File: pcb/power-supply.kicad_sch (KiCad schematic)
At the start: 10 parts, among them J1 Screw Connector, J2 Screw Connector, J3 Screw Connector, J4 Screw Connector, U9 NCP718BSNADJT1G

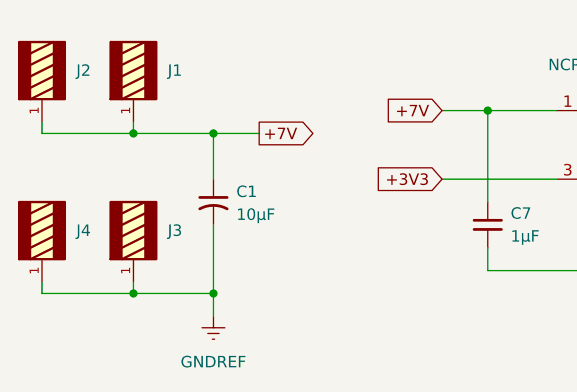
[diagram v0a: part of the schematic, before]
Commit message: Add header labels for UART and 3.3V
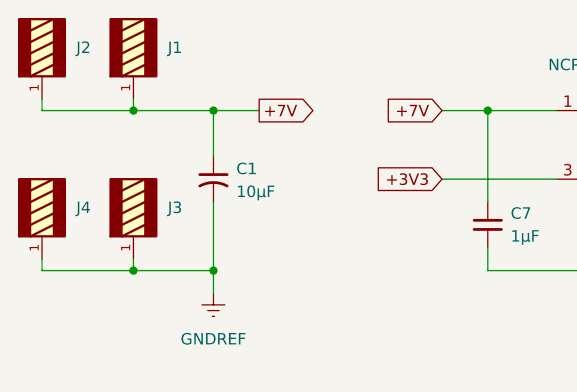
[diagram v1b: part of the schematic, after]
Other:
- company: (none) -> ECE 4710 - Vision Arm
- title: (none) -> 7V and 5V Power Supplies
- moved on the sheet: C1, J1, J2, J3, J4

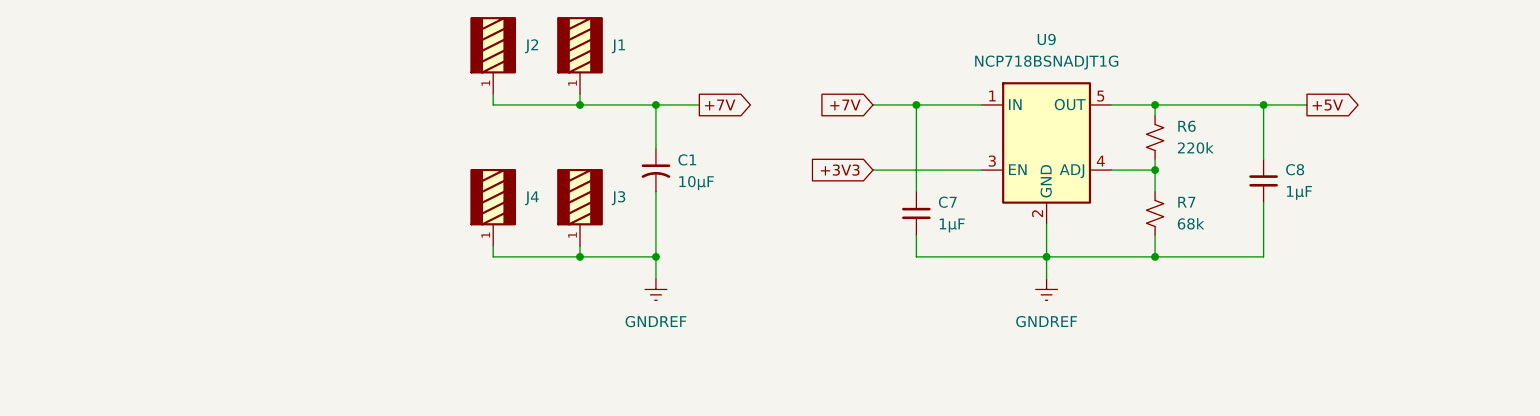
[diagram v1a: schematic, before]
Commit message: Add jumper to choose 3.3V or 7V for regulator enable
I'm not sure if using the 7V input voltage is alright, or if 7V is too
high. The datasheet for the LDO regulator `NCP718BSNADJT1G` doesn't seem
to make it clear, so the jumper lets us keep this same PCB design
without ordering a new board.
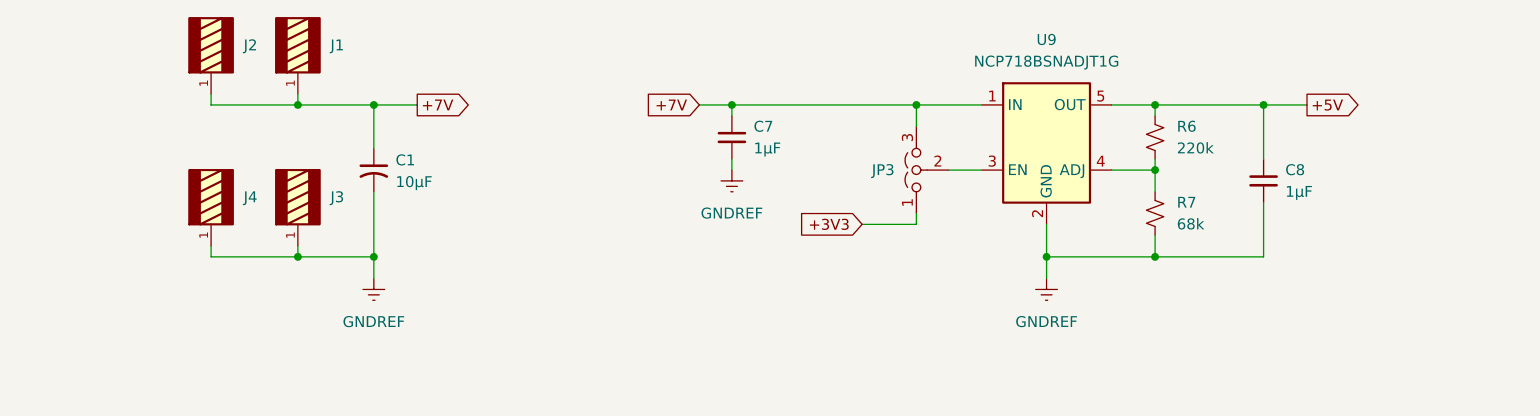
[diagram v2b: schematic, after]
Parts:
- added JP3: Jumper_3_Open, symbol Jumper:Jumper_3_Open
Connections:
- net +3V3: now also JP3.1 (A); no longer U9.3 (EN)
- net +7V: now also JP3.3 (B)
- new net: JP3.2 (C), U9.3 (EN)
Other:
- moved on the sheet: C1, J1, J2, J3, J4

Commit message: Change screw terminal to cheaper model
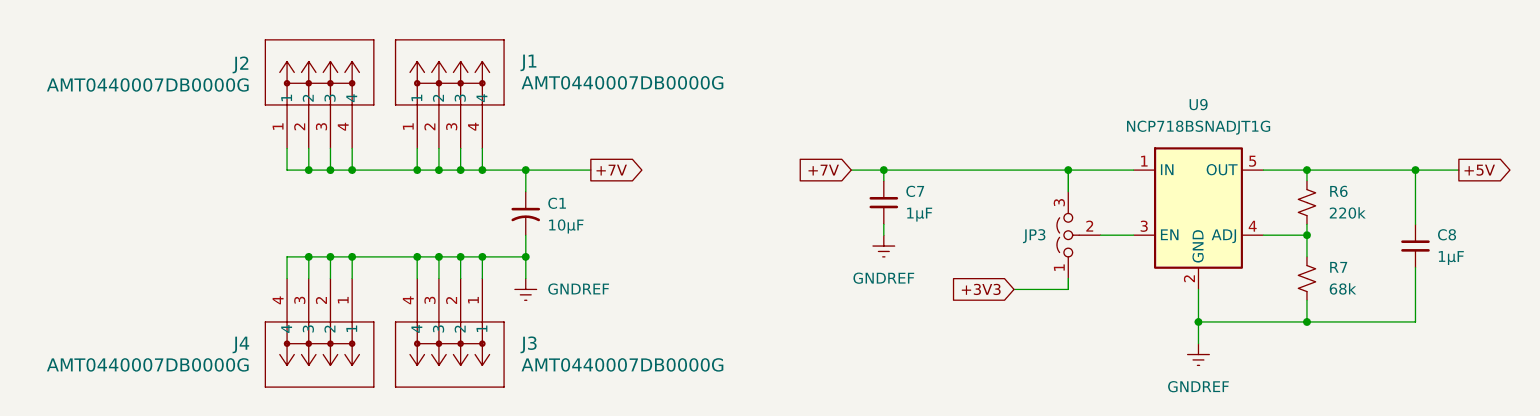
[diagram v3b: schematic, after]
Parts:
- removed J1, J2, J3, J4: Screw Connector, WP-THRBU_THROUGH-HOLE:WP-THRBU_74650074, symbol WP-THRBU_THROUGH-HOLE:WP-THRBU_THROUGH-HOLE
- added J1, J2, J3, J4: AMT0440007DB0000G, CONN_AMT0440007DB0000G_AMP, symbol AMT0440007DB0000G:AMT0440007DB0000G
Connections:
- net +7V: now also J1.1, J1.2, J1.3, J1.4, J2.1, J2.2, J2.3, J2.4
- net GNDREF: now also J3.1, J3.2, J3.3, J3.4, J4.1, J4.2, J4.3, J4.4
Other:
- moved on the sheet: C1, C7, C8, JP3, R6, R7, U9
